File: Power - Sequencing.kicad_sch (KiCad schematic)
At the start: 0 parts

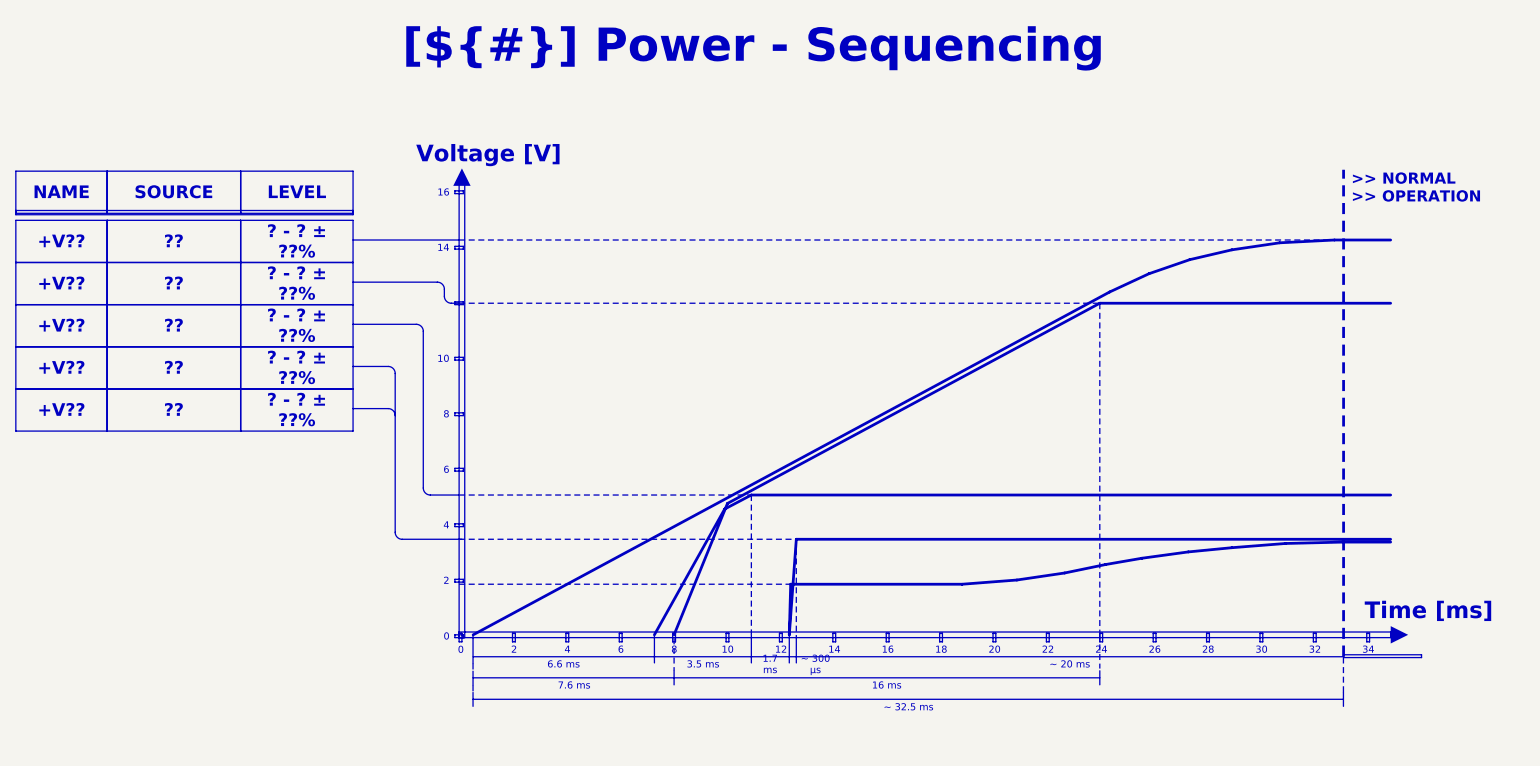
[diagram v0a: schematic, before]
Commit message: documentation update / block diagram
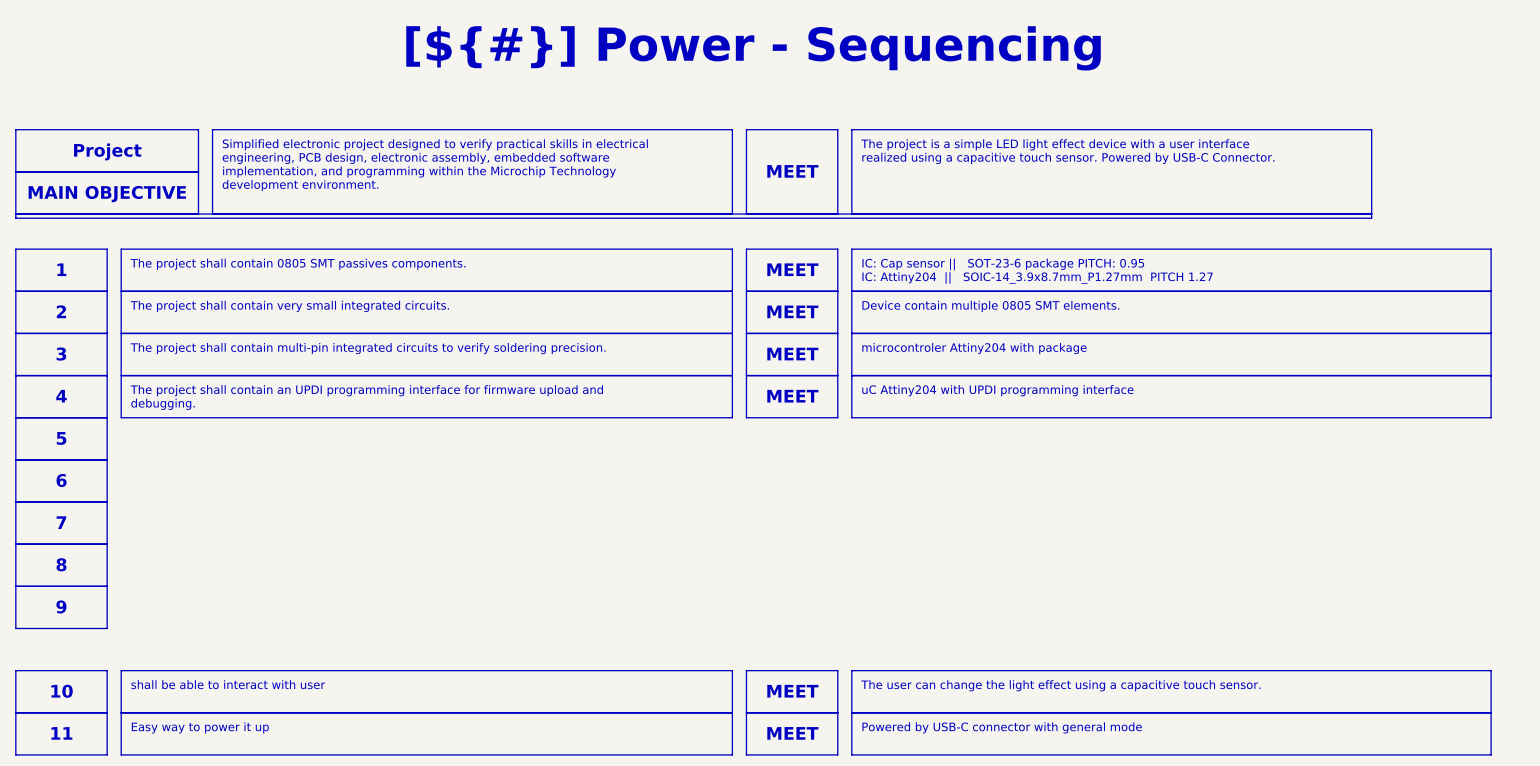
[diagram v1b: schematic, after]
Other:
- note removed: ">> NORMAL >> OPERATION"
- note removed: "Time [ms]"
- note removed: "Voltage [V]"
